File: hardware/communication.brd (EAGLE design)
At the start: 33.5 x 34.6 mm, 44 parts, among them J1 MICRO_USB_B_HIROSE_ZX62-B-5PA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, SW1 TVAF06-A020B-R, U2 NJM12888F, X1 FA-238

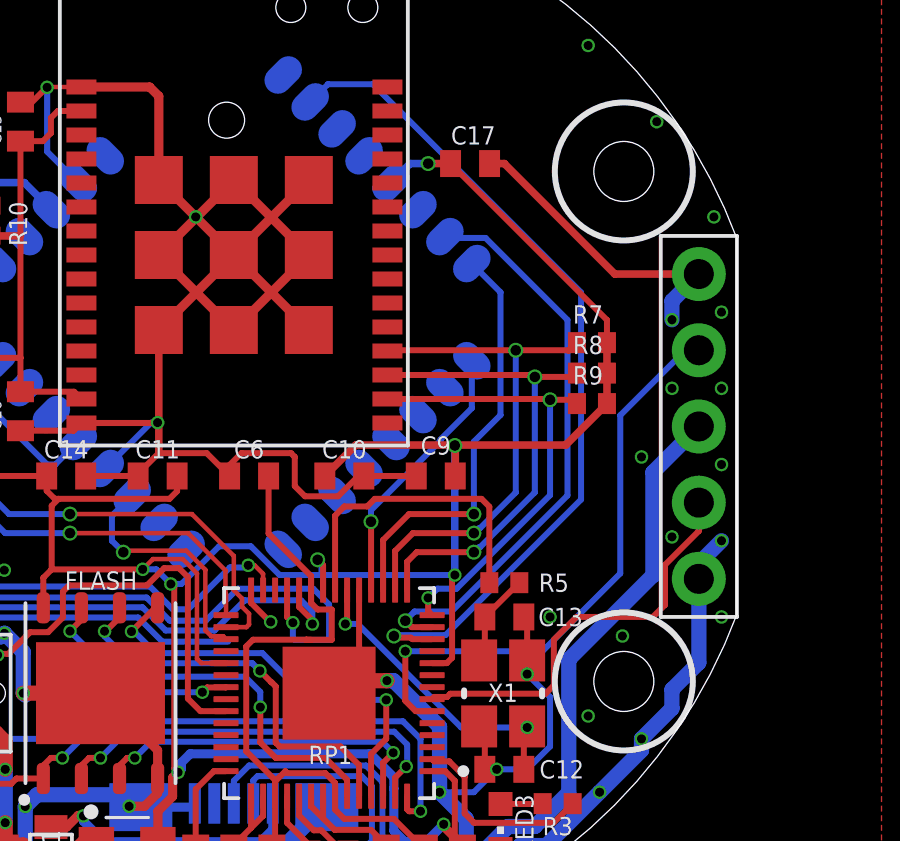
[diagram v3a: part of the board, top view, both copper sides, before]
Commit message: 変更点: communication_LoRaをUART接続に変換 gnss_GPSのRTX接続およびRESETの追加
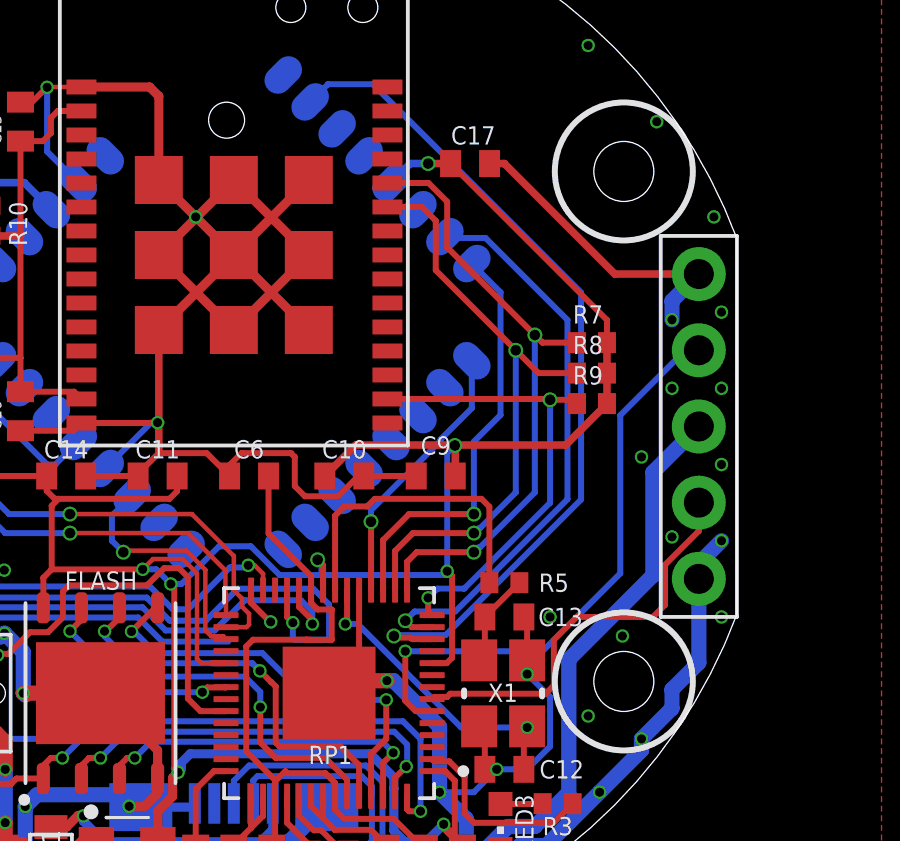
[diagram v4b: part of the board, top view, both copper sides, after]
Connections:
- removed net ROLA_SCL: R7.1, RP1.16, U$3.P19
- removed net ROLA_SDA: R8.1, RP1.15, U$3.P18
- new net ROLA_RTX: R8.1, RP1.16, U$3.P25
- new net ROLA_TRX: R7.1, RP1.15, U$3.P26
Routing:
- net ROLA_TRX: track 0.00 -> 20.8 mm, vias 0 -> 2
- net ROLA_RTX: track 0.00 -> 20.5 mm, vias 0 -> 2
- net ROLA_SCL: track 17.7 -> 0.00 mm, vias 2 -> 0
- net ROLA_SDA: track 16.5 -> 0.00 mm, vias 2 -> 0
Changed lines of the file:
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@@
 <wire x1="-1.27" y1="-14.605" x2="-2.286" y2="-14.605" width="0.3048" layer="1"/>
 <wire x1="7.381" y1="-1.651" x2="7.366" y2="-1.666" width="0.2" layer="1"/>
-<wire x1="7.366" y1="-4.953" x2="7.2755" y2="-5.0435" width="0.2" layer="1"/>
-<wire x1="7.2755" y1="-5.0435" x2="7.2755" y2="-7.7105" width="0.2" layer="1"/>
 <wire x1="7.2755" y1="-7.7105" x2="7.096" y2="-7.89" width="0.2" layer="1"/>
 <wire x1="7.096" y1="-7.89" x2="6.61" y2="-7.89" width="0.2" layer="1"/>
@@
 <wire x1="7.62" y1="-13.955" x2="7.62" y2="-14.351" width="0.3048" layer="1"/>
 <wire x1="2.975" y1="-12.325" x2="2.975" y2="-13.06155" width="0.2" layer="1"/>
-<via x="7.366" y="-4.953" extent="1-16" drill="0.3"/>
+<via x="7.112" y="-4.826" extent="1-16" drill="0.3"/>
 <wire x1="-0.4925" y1="-3.9955" x2="0.5685" y2="-3.9955" width="0.2" layer="16"/>
 <wire x1="0.5685" y1="-3.9955" x2="1.526" y2="-4.953" width="0.2" layer="16"/>
@@
 <contactref element="R9" pad="2"/>
 <wire x1="-7.112" y1="2.286" x2="-7.112" y2="1.158" width="0.2" layer="1"/>
-<wire x1="7.366" y1="-0.635" x2="7.366" y2="-4.953" width="0.254" layer="16"/>
 <contactref element="U$1" pad="5"/>
 <contactref element="C17" pad="1"/>
@@
 <wire x1="7.381" y1="-0.62" x2="11.064" y2="-0.62" width="0.254" layer="1"/>
 <wire x1="1.526" y1="-4.953" x2="2.921" y2="-4.953" width="0.2" layer="16"/>
-<wire x1="2.921" y1="-4.953" x2="7.366" y2="-4.953" width="0.2" layer="16"/>
 <wire x1="-6.35" y1="-6.045" x2="-6.35" y2="-5.044" width="0.2" layer="1"/>
 <wire x1="-6.35" y1="-5.044" x2="-6.071" y2="-4.765" width="0.2" layer="1"/>
@@
 <wire x1="-2.0995" y1="-5.25" x2="-1.747" y2="-5.25" width="0.2" layer="16"/>
 <wire x1="-1.747" y1="-5.25" x2="-0.4925" y2="-3.9955" width="0.2" layer="16"/>
+<wire x1="7.112" y1="-4.826" x2="7.2755" y2="-4.9895" width="0.2" layer="1"/>
+<wire x1="7.2755" y1="-4.9895" x2="7.2755" y2="-7.7105" width="0.2" layer="1"/>
+<wire x1="2.921" y1="-4.953" x2="6.985" y2="-4.953" width="0.2" layer="16"/>
+<wire x1="6.985" y1="-4.953" x2="7.112" y2="-4.826" width="0.2" layer="16"/>
+<wire x1="7.366" y1="-0.635" x2="7.112" y2="-0.889" width="0.2" layer="16"/>
+<wire x1="7.112" y1="-0.889" x2="7.112" y2="-4.826" width="0.2" layer="16"/>
 <wire x1="7.366" y1="-0.635" x2="7.381" y2="-1.651" width="0" layer="19" extent="1-1"/>
 </signal>
@@
 <wire x1="6.477" y1="-6.157" x2="6.477" y2="-5.715" width="0.2" layer="1"/>
 <wire x1="6.477" y1="-5.715" x2="6.7858" y2="-5.4062" width="0.2" layer="16"/>
-<wire x1="6.7858" y1="-5.4062" x2="7.426725" y2="-5.4062" width="0.2" layer="16"/>
-<wire x1="7.426725" y1="-5.4062" x2="10.541" y2="-2.291925" width="0.2" layer="16"/>
-<wire x1="10.541" y1="-2.291925" x2="10.541" y2="0.889" width="0.2" layer="16"/>
+<wire x1="6.7858" y1="-5.4062" x2="7.680725" y2="-5.4062" width="0.2" layer="16"/>
+<wire x1="7.680725" y1="-5.4062" x2="10.541" y2="-2.545925" width="0.2" layer="16"/>
+<wire x1="10.541" y1="-2.545925" x2="10.541" y2="0.889" width="0.2" layer="16"/>
 <via x="10.541" y="0.889" extent="1-16" drill="0.35"/>
 <wire x1="5.12" y1="0.915" x2="10.515" y2="0.915" width="0.2" layer="1"/>
@@
 <wire x1="10.541" y1="0.889" x2="11.311" y2="0.889" width="0.2" layer="1"/>
 <wire x1="11.311" y1="0.889" x2="11.438" y2="0.762" width="0.2" layer="1"/>
-</signal>
-<signal name="ROLA_SCL">
-<contactref element="R7" pad="1"/>
-<contactref element="U$3" pad="P19"/>
-<contactref element="RP1" pad="16"/>
-<wire x1="11.159" y1="2.515" x2="11.438" y2="2.794" width="0.2032" layer="1"/>
-<via x="8.001" y="-3.556" extent="1-16" drill="0.35"/>
-<wire x1="8.001" y1="-3.556" x2="5.969" y2="-3.556" width="0.2" layer="1"/>
-<wire x1="5.969" y1="-3.556" x2="5.375" y2="-4.15" width="0.2" layer="1"/>
-<wire x1="5.375" y1="-4.15" x2="5.375" y2="-5.455" width="0.2" layer="1"/>
-<wire x1="8.001" y1="-3.556" x2="8.1578" y2="-3.3992" width="0.2" layer="16"/>
-<wire x1="8.1578" y1="-3.3992" x2="8.19908125" y2="-3.3992" width="0.2" layer="16"/>
-<wire x1="8.19908125" y1="-3.3992" x2="9.398" y2="-2.20028125" width="0.2" layer="16"/>
-<wire x1="9.398" y1="-2.20028125" x2="9.398" y2="2.54" width="0.2" layer="16"/>
-<via x="9.398" y="2.54" extent="1-16" drill="0.35"/>
-<wire x1="5.12" y1="2.515" x2="5.145" y2="2.54" width="0.2" layer="1"/>
-<wire x1="5.145" y1="2.54" x2="9.398" y2="2.54" width="0.2" layer="1"/>
-<wire x1="9.398" y1="2.54" x2="11.184" y2="2.54" width="0.2" layer="1"/>
-<wire x1="11.184" y1="2.54" x2="11.438" y2="2.794" width="0.2" layer="1"/>
-</signal>
-<signal name="ROLA_SDA">
-<contactref element="R8" pad="1"/>
-<contactref element="U$3" pad="P18"/>
-<wire x1="11.438" y1="1.778" x2="11.437125" y2="1.778875" width="0.3048" layer="1"/>
-<contactref element="RP1" pad="15"/>
-<wire x1="11.375" y1="1.715" x2="11.438" y2="1.778" width="0.2032" layer="1"/>
-<via x="8.001" y="-4.191" extent="1-16" drill="0.35"/>
-<wire x1="5.775" y1="-5.455" x2="5.775" y2="-4.512" width="0.2" layer="1"/>
-<wire x1="5.775" y1="-4.512" x2="6.096" y2="-4.191" width="0.2" layer="1"/>
-<wire x1="6.096" y1="-4.191" x2="8.001" y2="-4.191" width="0.2" layer="1"/>
-<wire x1="8.001" y1="-4.191" x2="8.1578" y2="-4.0342" width="0.2" layer="16"/>
-<wire x1="8.1578" y1="-4.0342" x2="8.19908125" y2="-4.0342" width="0.2" layer="16"/>
-<wire x1="8.19908125" y1="-4.0342" x2="10.033" y2="-2.20028125" width="0.2" layer="16"/>
-<wire x1="10.033" y1="-2.20028125" x2="10.033" y2="1.651" width="0.2" layer="16"/>
-<via x="10.033" y="1.651" extent="1-16" drill="0.35"/>
-<wire x1="5.12" y1="1.715" x2="9.969" y2="1.715" width="0.2" layer="1"/>
-<wire x1="9.969" y1="1.715" x2="10.033" y2="1.651" width="0.2" layer="1"/>
-<wire x1="10.033" y1="1.651" x2="11.311" y2="1.651" width="0.2" layer="1"/>
-<wire x1="11.311" y1="1.651" x2="11.438" y2="1.778" width="0.2" layer="1"/>
 </signal>
 <signal name="TWE_RTX">
@@
 <wire x1="5.928" y1="-6.69" x2="5.715" y2="-6.477" width="0.2" layer="1"/>
 <wire x1="5.715" y1="-6.477" x2="6.0238" y2="-6.1682" width="0.2" layer="16"/>
-<wire x1="6.0238" y1="-6.1682" x2="7.254175" y2="-6.1682" width="0.2" layer="16"/>
-<wire x1="7.254175" y1="-6.1682" x2="11.1212" y2="-2.301175" width="0.2" layer="16"/>
+<wire x1="6.0238" y1="-6.1682" x2="7.381175" y2="-6.1682" width="0.2" layer="16"/>
+<wire x1="7.381175" y1="-6.1682" x2="11.1212" y2="-2.428175" width="0.2" layer="16"/>
 <wire x1="7.0794" y1="6.283046875" x2="7.035146875" y2="6.3273" width="0.2" layer="16"/>
 <wire x1="8.390375" y1="6.283046875" x2="7.0794" y2="6.283046875" width="0.2" layer="16"/>
-<wire x1="11.1212" y1="-2.301175" x2="11.1212" y2="3.552221875" width="0.2" layer="16"/>
+<wire x1="11.1212" y1="-2.428175" x2="11.1212" y2="3.552221875" width="0.2" layer="16"/>
 <wire x1="11.1212" y1="3.552221875" x2="8.390375" y2="6.283046875" width="0.2" layer="16"/>
 </signal>
@@
 <wire x1="-4.064" y1="-3.81" x2="-3.683" y2="-4.191" width="0.2" layer="16"/>
 </signal>
+<signal name="ROLA_TRX">
+<contactref element="U$3" pad="P26"/>
+<contactref element="R7" pad="1"/>
+<contactref element="RP1" pad="15"/>
+<via x="8.001" y="-4.191" extent="1-16" drill="0.35"/>
+<wire x1="5.775" y1="-5.455" x2="5.775" y2="-4.512" width="0.2" layer="1"/>
+<wire x1="5.775" y1="-4.512" x2="6.096" y2="-4.191" width="0.2" layer="1"/>
+<wire x1="6.096" y1="-4.191" x2="8.001" y2="-4.191" width="0.2" layer="1"/>
+<wire x1="8.001" y1="-4.191" x2="8.1578" y2="-4.0342" width="0.2" layer="16"/>
+<wire x1="8.1578" y1="-4.0342" x2="8.19908125" y2="-4.0342" width="0.2" layer="16"/>
+<wire x1="8.19908125" y1="-4.0342" x2="10.033" y2="-2.20028125" width="0.2" layer="16"/>
+<wire x1="10.033" y1="-2.20028125" x2="10.033" y2="3.048" width="0.2" layer="16"/>
+<via x="10.033" y="3.048" extent="1-16" drill="0.35"/>
+<wire x1="5.12" y1="8.115" x2="6.49" y2="8.115" width="0.2" layer="1"/>
+<wire x1="6.49" y1="8.115" x2="7.112" y2="7.493" width="0.2" layer="1"/>
+<wire x1="7.112" y1="7.493" x2="7.112" y2="5.969" width="0.2" layer="1"/>
+<wire x1="7.112" y1="5.969" x2="10.033" y2="3.048" width="0.2" layer="1"/>
+<wire x1="10.033" y1="3.048" x2="10.287" y2="2.794" width="0.2" layer="1"/>
+<wire x1="10.287" y1="2.794" x2="11.438" y2="2.794" width="0.2" layer="1"/>
+</signal>
+<signal name="ROLA_RTX">
+<contactref element="U$3" pad="P25"/>
+<contactref element="R8" pad="1"/>
+<contactref element="RP1" pad="16"/>
+<via x="8.001" y="-3.556" extent="1-16" drill="0.35"/>
+<wire x1="8.001" y1="-3.556" x2="5.969" y2="-3.556" width="0.2" layer="1"/>
+<wire x1="5.969" y1="-3.556" x2="5.375" y2="-4.15" width="0.2" layer="1"/>
+<wire x1="5.375" y1="-4.15" x2="5.375" y2="-5.455" width="0.2" layer="1"/>
+<wire x1="8.001" y1="-3.556" x2="8.1578" y2="-3.3992" width="0.2" layer="16"/>
+<wire x1="8.1578" y1="-3.3992" x2="8.19908125" y2="-3.3992" width="0.2" layer="16"/>
+<wire x1="8.19908125" y1="-3.3992" x2="9.398" y2="-2.20028125" width="0.2" layer="16"/>
+<wire x1="9.398" y1="-2.20028125" x2="9.398" y2="2.54" width="0.2" layer="16"/>
+<via x="9.398" y="2.54" extent="1-16" drill="0.35"/>
+<wire x1="5.12" y1="7.315" x2="6.274" y2="7.315" width="0.2" layer="1"/>
+<wire x1="6.731" y1="5.207" x2="9.398" y2="2.54" width="0.2" layer="1"/>
+<wire x1="6.274" y1="7.315" x2="6.731" y2="6.858" width="0.2" layer="1"/>
+<wire x1="6.731" y1="6.858" x2="6.731" y2="5.207" width="0.2" layer="1"/>
+<wire x1="9.398" y1="2.54" x2="10.16" y2="1.778" width="0.2" layer="1"/>
+<wire x1="10.16" y1="1.778" x2="11.438" y2="1.778" width="0.2" layer="1"/>
+</signal>
 </signals>

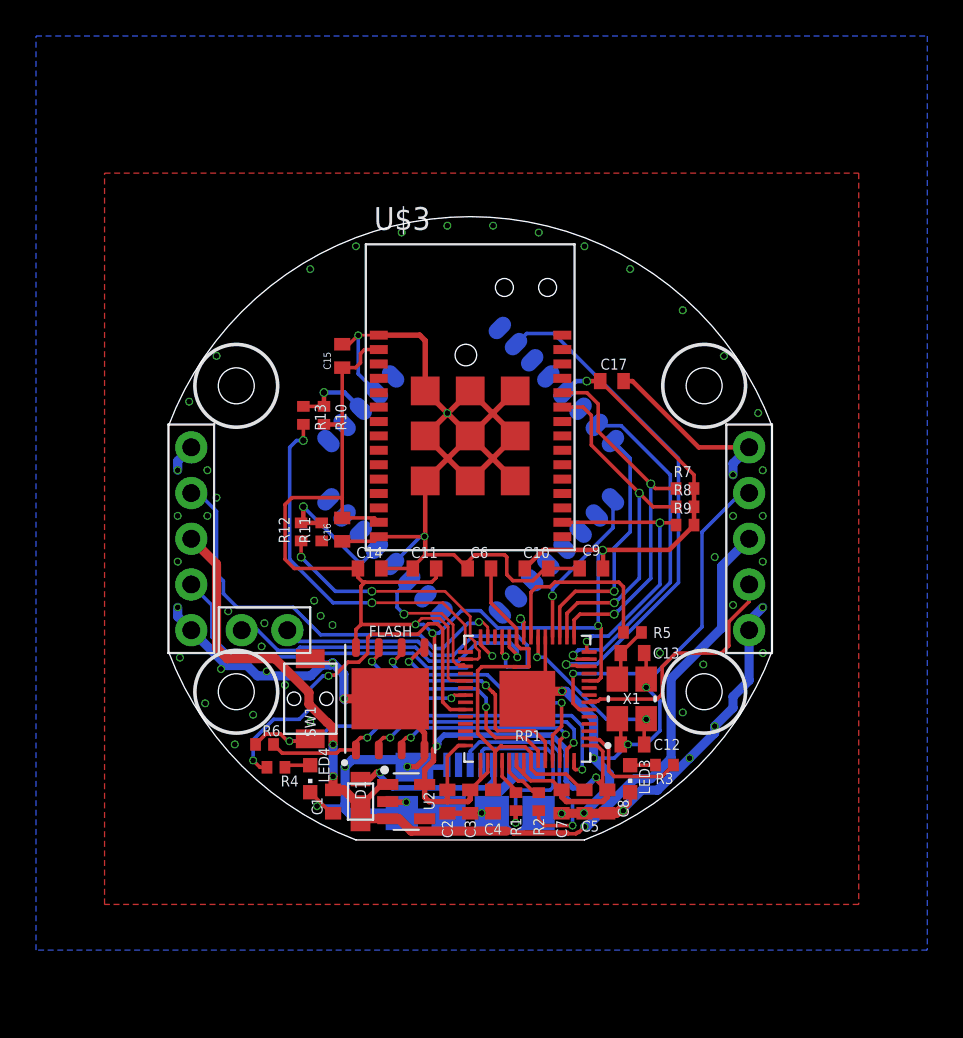
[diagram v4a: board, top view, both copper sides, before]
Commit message: べたGND前です。esp32のschはノータッチなのでここに上がってないです。よろしくお願いします。
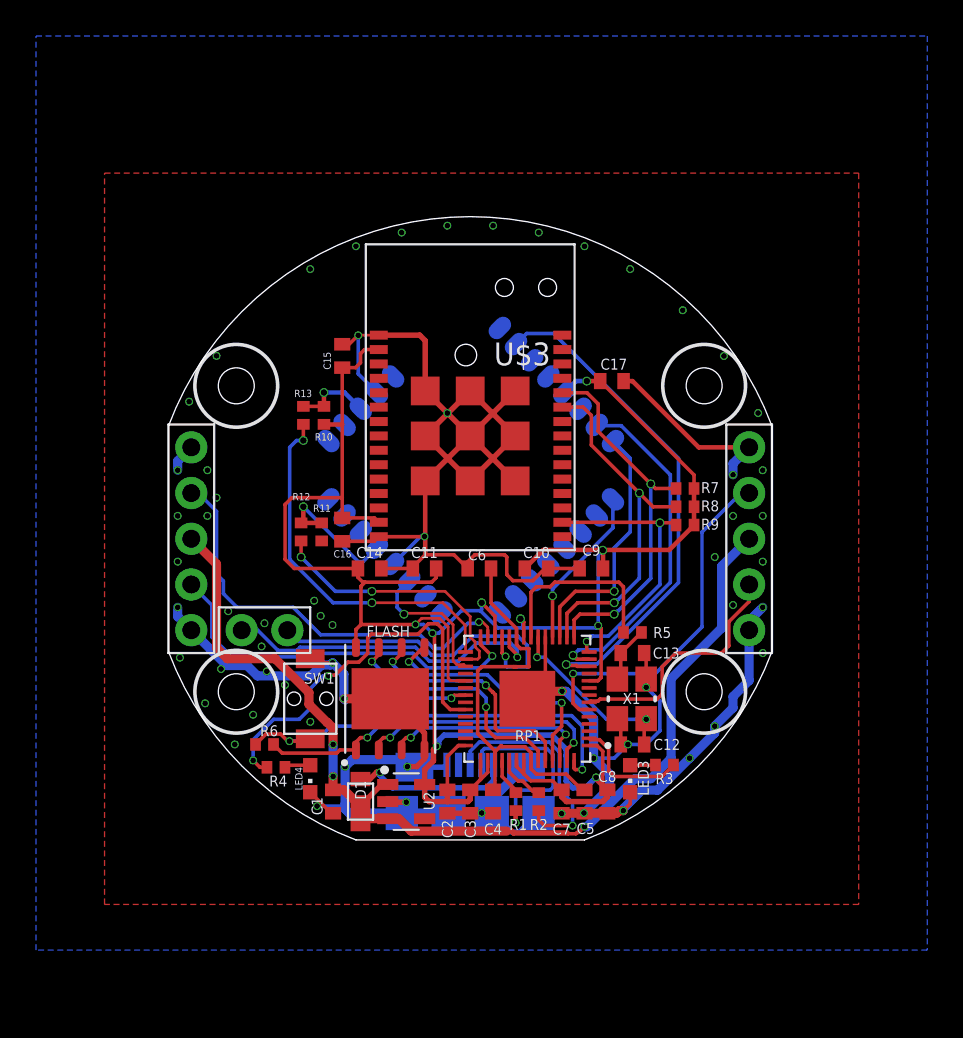
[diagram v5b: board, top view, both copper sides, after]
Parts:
- C12, C13, C14: value (none) -> 0.1μ
- C5, C6: value (none) -> 1μ
- R1, R2: value (none) -> 27Ω
- R3, R4: value (none) -> 1k
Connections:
- removed net ADC0: RP1.38
- removed net ADC1: RP1.39
- removed net ADC2: RP1.40
- removed net ADC3: RP1.41
- removed net I2C0_SDA: RP1.11
- removed net I2C1_SCL: RP1.9
- removed net I2C1_SDA: RP1.8
- removed net PWM0_B: RP1.3
- removed net PWM1_A: RP1.4
- removed net PWM1_B: RP1.5
- removed net PWM3_A: RP1.34
- removed net PWM4_A: RP1.36
- removed net SPI0_CS: RP1.32
- net VDD: now also RP1.26
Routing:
- net VDD: track 131.6 -> 134.3 mm, vias 8 -> 9
- net RX0: track 19.8 -> 21.5 mm
- net GND: vias 65 -> 62
